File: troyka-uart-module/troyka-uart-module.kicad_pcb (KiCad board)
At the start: 2 copper layers, 25.4 x 25.4 mm, 5 parts, among them J1 UP (A), J2 DOWN (A)

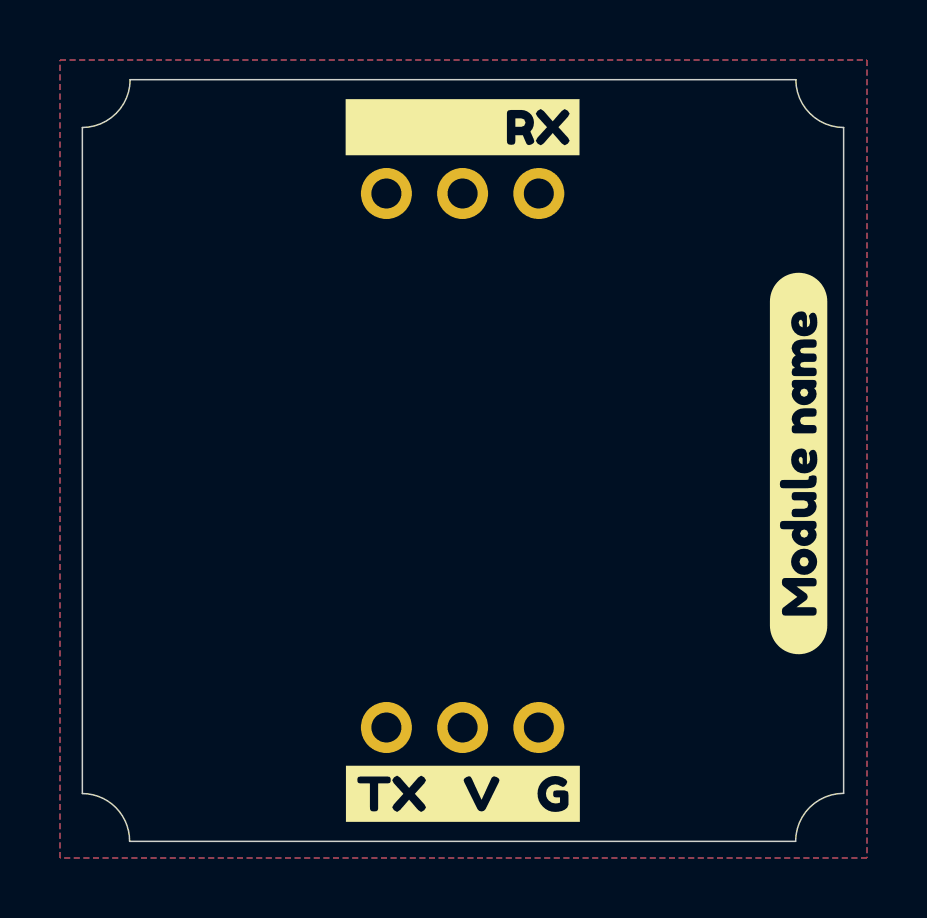
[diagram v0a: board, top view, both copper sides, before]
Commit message: Update templates and CI
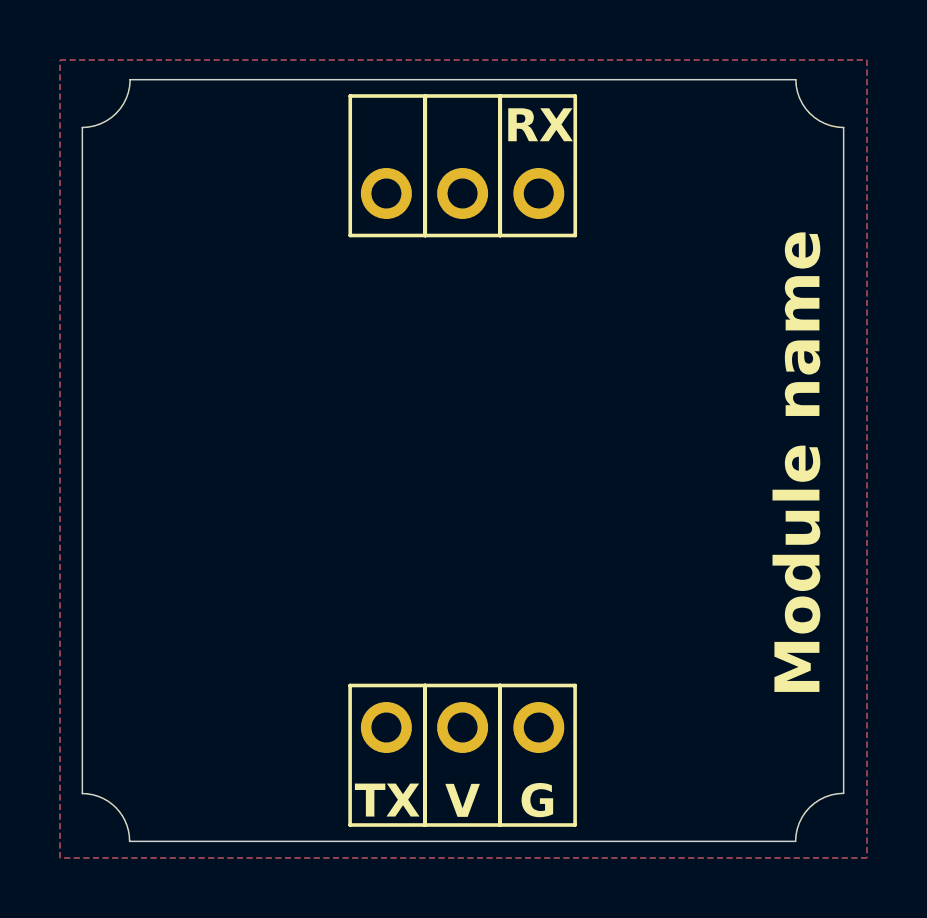
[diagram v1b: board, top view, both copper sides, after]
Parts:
- removed kibuzzard-63E392E0: G***, kibuzzard-63E392E0
- removed kibuzzard-63E396F1: G***, kibuzzard-63E396F1
- removed kibuzzard-63E39710: G***, kibuzzard-63E39710
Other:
- board text added: "G"
- board text added: "Module name"
- board text added: "RX"
- board text added: "TX"
- board text added: "V"
